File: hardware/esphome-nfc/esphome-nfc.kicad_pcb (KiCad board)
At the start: 4 copper layers, 68.2 x 41 mm, 20 parts, among them U1 ESP32-C3-WROOM-02, U2 PN7160A1HN/C100Y, U3 AMS1117-3.3, Y1 Crystal_GND24

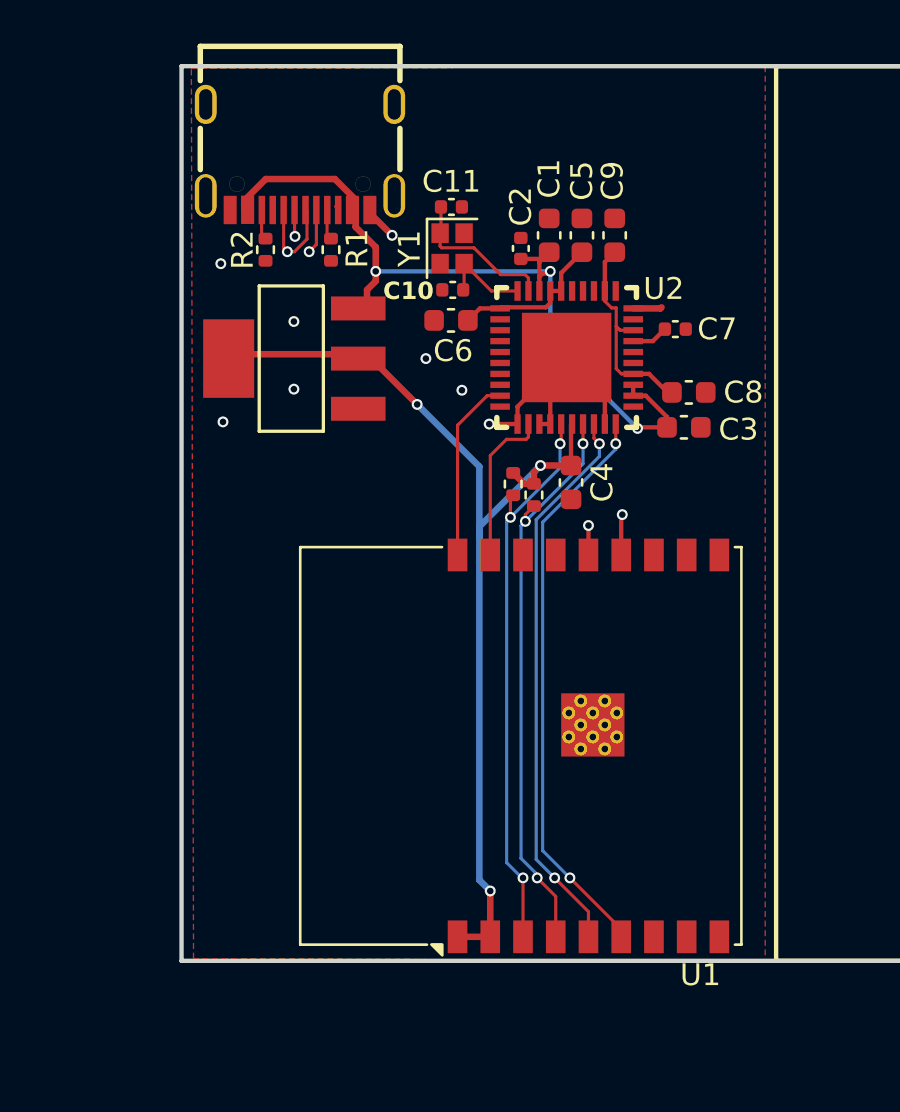
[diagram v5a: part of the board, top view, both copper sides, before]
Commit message: esphome-nfc: route & finalize everything except for NFC antenna and corresponding matching circuit
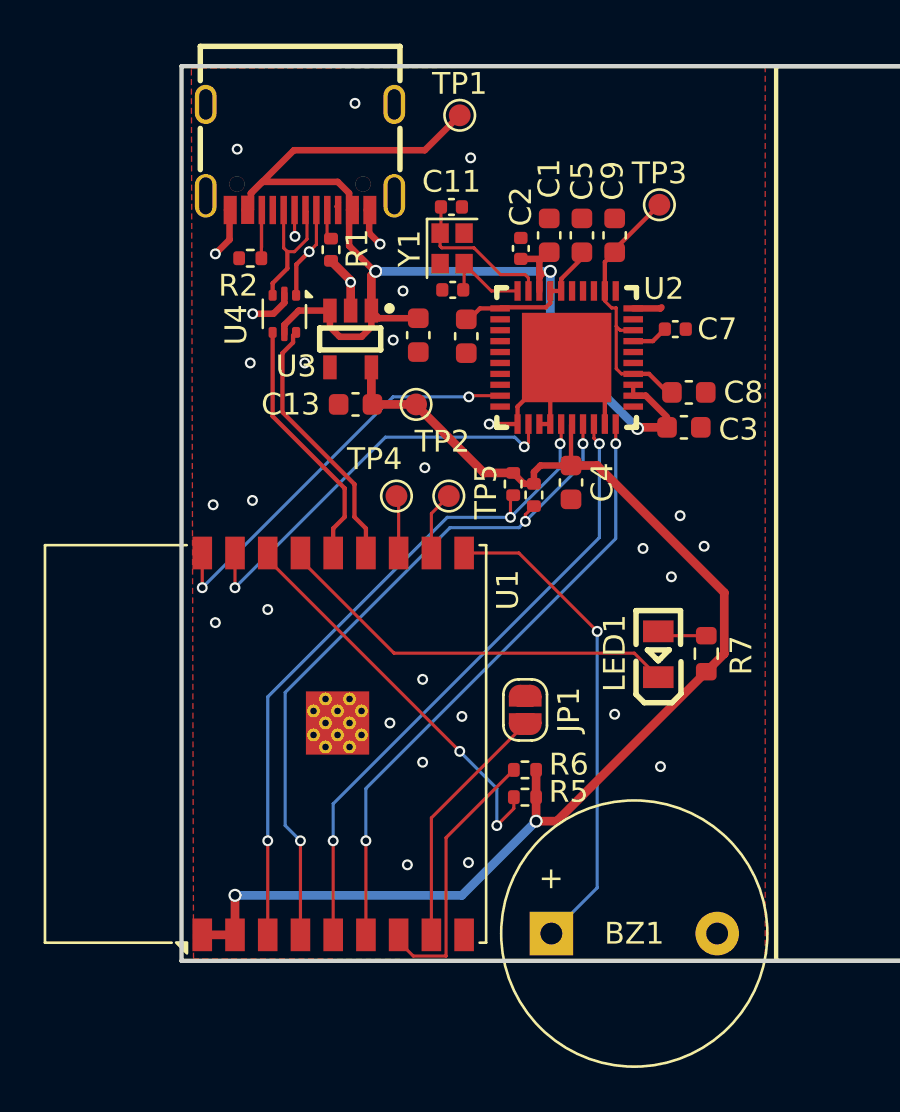
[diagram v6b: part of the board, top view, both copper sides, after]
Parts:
- added BZ1: Buzzer, Buzzer_Beeper:Buzzer_12x9.5RM7.6, F.Cu at (173.2, 113.8)
- added C12: 1.0 uF, Capacitor_SMD:C_0603_1608Metric, F.Cu at (167.1, 86.3)
- added C13: 1.0 uF, Capacitor_SMD:C_0603_1608Metric, F.Cu at (164.2, 89.5)
- added JP1: SolderJumper_2_Open, Jumper:SolderJumper-2_P1.3mm_Open_RoundedPad1.0x1.5mm, F.Cu at (172.0, 103.5)
- added LED1: 0805G (Green), easyeda2kicad:LED0805-R-RD, F.Cu at (178.1, 101.0)
- added R5: 10k, Resistor_SMD:R_0402_1005Metric, F.Cu at (172.0, 107.5)
- added R6: 10k, Resistor_SMD:R_0402_1005Metric, F.Cu at (172.0, 106.2)
- added R7: 100R, Resistor_SMD:R_0603_1608Metric, F.Cu at (180.3, 100.9)
- added TP1: ~, TestPoint:TestPoint_Pad_D1.0mm, F.Cu at (169.0, 76.2)
- added TP2: ~, TestPoint:TestPoint_Pad_D1.0mm, F.Cu at (167.0, 89.5)
- added TP3: ~, TestPoint:TestPoint_Pad_D1.0mm, F.Cu at (178.2, 80.3)
- added TP4: ~, TestPoint:TestPoint_Pad_D1.0mm, F.Cu at (166.1, 93.7)
- added TP5: ~, TestPoint:TestPoint_Pad_D1.0mm, F.Cu at (168.5, 93.7)
- added U4: USBLC6-2P6, Package_TO_SOT_SMD:SOT-666, F.Cu at (161.0, 85.3)
- U3: value AMS1117-3.3 -> AP2112K-3.3TRG1; footprint easyeda2kicad:SOT-223-3_L6.5-W3.4-P2.30-LS7.0-BR -> easyeda2kicad:SOT-25-5_L2.9-W1.6-P0.95-LS2.8-BL
- moved U1 11.7 mm to (163.2, 105.1)
- moved U3 2.77 mm to (164.0, 86.5), turned to 180 degrees
- moved C6 1.01 mm to (169.3, 86.4), turned to -90 degrees
- moved R2 0.80 mm to (159.4, 82.8), turned to 180 degrees
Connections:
- U1 pad 10: unconnected-(U1-IO10-Pad10) -> /BUZZER
- U1 pad 11: unconnected-(U1-IO20/RXD-Pad11) -> Net-(U1-IO20/RXD)
- U1 pad 12: unconnected-(U1-IO21/TXD-Pad12) -> Net-(U1-IO21/TXD)
- U1 pad 15: unconnected-(U1-IO3-Pad15) -> /LED
- U1 pad 16: unconnected-(U1-IO2-Pad16) -> Net-(U1-IO2)
- U1 pad 7: unconnected-(U1-IO8-Pad7) -> Net-(U1-IO8)
- U1 pad 8: unconnected-(U1-IO9-Pad8) -> Net-(JP1-A)
- U3 pad 1: GND -> +5V
- U3 pad 2: +3V3 -> GND
- U3 pad 4: +3V3 -> unconnected-(U3-NC-Pad4)
- USB2 pad 1: GND -> unconnected-(USB2-EP-Pad1)
- USB2 pad 2: GND -> unconnected-(USB2-EP-Pad2)
- USB2 pad 3: GND -> unconnected-(USB2-EP-Pad3)
- USB2 pad 4: GND -> unconnected-(USB2-EP-Pad4)
- USB2 pad A6: /D+ -> /DP
- USB2 pad A7: /D- -> /DN
- USB2 pad B6: /D+ -> /DP
- USB2 pad B7: /D- -> /DN
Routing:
- net /BUZZER: track 0.00 -> 22.3 mm, vias 0 -> 1
- net +5V: track 37.8 -> 57.5 mm
- net /LED: track 0.00 -> 18.9 mm
- net Net-(U1-IO2): track 0.00 -> 18.5 mm, vias 0 -> 2
- net /D+: track 26.1 -> 11.7 mm, vias 2 -> 0
- net /D-: track 25.9 -> 12.0 mm, vias 3 -> 0
- net +3V3: track 46.7 -> 59.8 mm, vias 3 -> 2
- net Net-(U1-IO8): track 0.00 -> 12.6 mm
- net /NFC_DWL: track 7.25 -> 19.0 mm, vias 0 -> 2
- net Net-(JP1-A): track 0.00 -> 11.4 mm
- net /NFC_WKUP: track 8.46 -> 18.9 mm, vias 0 -> 2
- net GND: track 16.1 -> 23.1 mm, vias 8 -> 29
- net /DP: track 0.00 -> 6.76 mm
- net /DN: track 0.00 -> 6.48 mm, vias 0 -> 2
- net /NFC_SCL: track 26.2 -> 32.1 mm
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
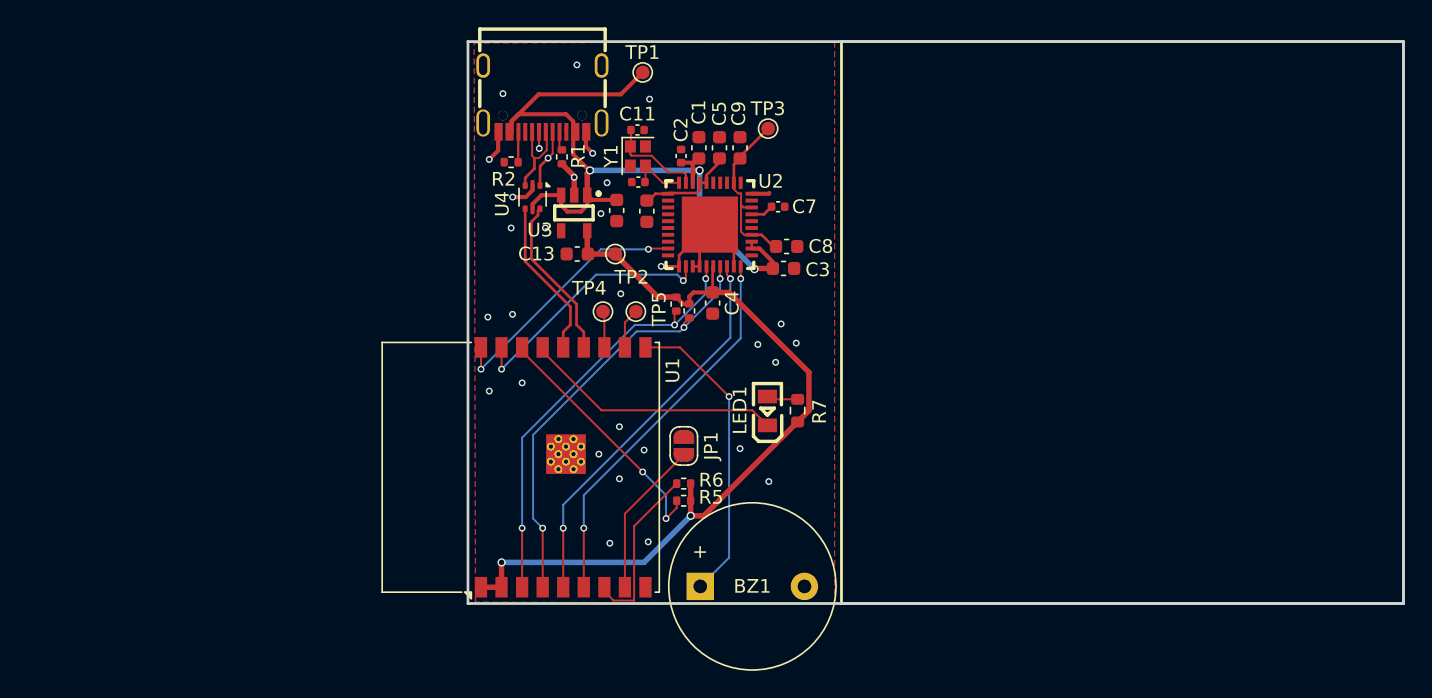
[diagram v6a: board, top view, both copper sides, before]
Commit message: esphome-nfc final touches
* Add an antenna and corresponding matching circuitry
* Add a button (you never know...)
* Mark components I plan to solder manually as "Do Not Place"
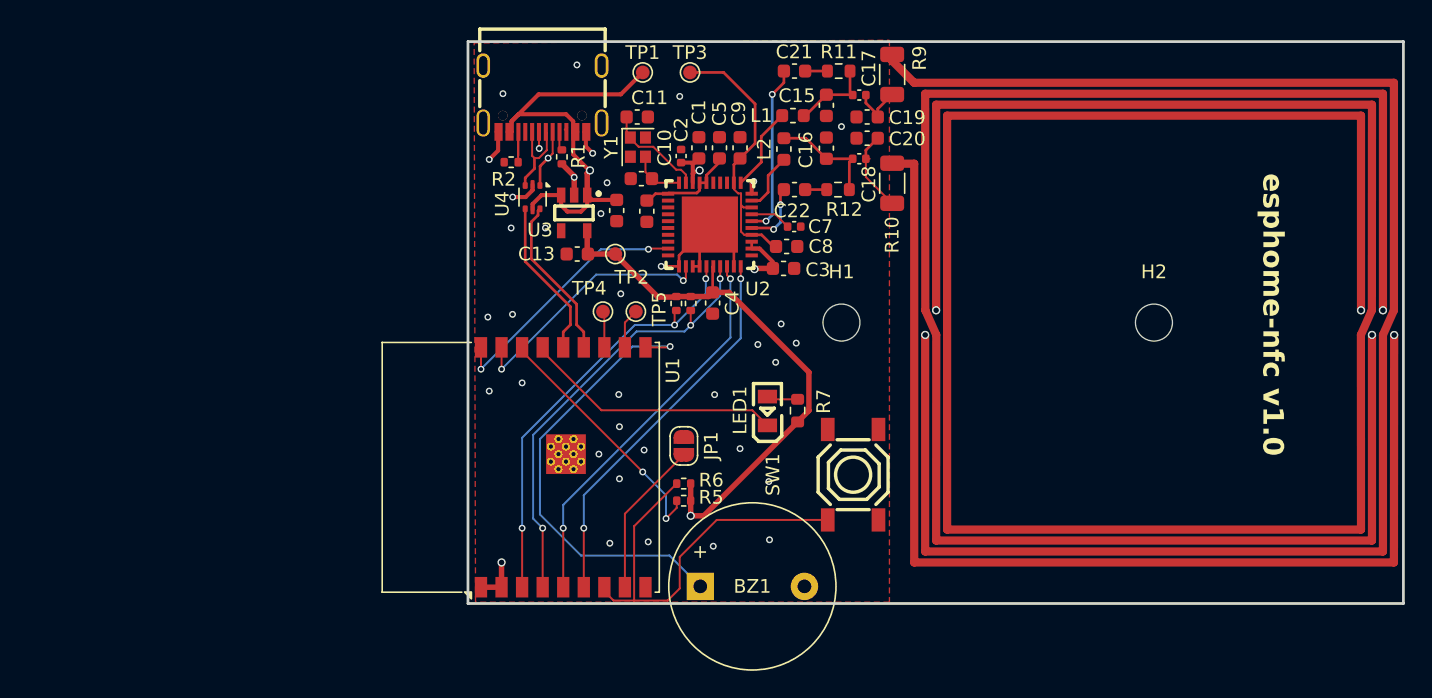
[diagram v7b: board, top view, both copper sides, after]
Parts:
- added C15: 330 pF, Capacitor_SMD:C_0603_1608Metric, F.Cu at (182.4, 78.7)
- added C16: 330 pF, Capacitor_SMD:C_0603_1608Metric, F.Cu at (182.4, 81.8)
- added C17: 75 pF, Capacitor_SMD:C_0402_1005Metric, F.Cu at (184.8, 77.9)
- added C18: 75 pF, Capacitor_SMD:C_0402_1005Metric, F.Cu at (184.8, 82.5)
- added C19: 150 pF, Capacitor_SMD:C_0603_1608Metric, F.Cu at (185.4, 79.5)
- added C20: 150 pF, Capacitor_SMD:C_0603_1608Metric, F.Cu at (185.4, 81.0)
- added C21: 1.0 uF, Capacitor_SMD:C_0603_1608Metric, F.Cu at (180.1, 76.2)
- added C22: 1.0 uF, Capacitor_SMD:C_0603_1608Metric, F.Cu at (180.1, 84.8)
- added H1: MountingHole, MountingHole:MountingHole_2.7mm_M2.5, F.Cu at (183.5, 94.5)
- added H2: MountingHole, MountingHole:MountingHole_2.7mm_M2.5, F.Cu at (206.3, 94.5)
- added L1: 160 nH, Inductor_SMD:L_0603_1608Metric, F.Cu at (180.0, 79.4)
- added L2: 160 nH, Inductor_SMD:L_0603_1608Metric, F.Cu at (179.3, 81.8)
- added R10: 2R0, Resistor_SMD:R_1206_3216Metric, F.Cu at (187.2, 84.3)
- added R11: 2.2K, Resistor_SMD:R_0603_1608Metric, F.Cu at (183.3, 76.2)
- added R12: 2.2K, Resistor_SMD:R_0603_1608Metric, F.Cu at (183.2, 84.8)
- added R9: 2R0, Resistor_SMD:R_1206_3216Metric, F.Cu at (187.2, 76.4)
- added SW1: TS-1187A-B-A-B, easyeda2kicad:SW-SMD_4P-L5.1-W5.1-P3.70-LS6.5-TL-2, F.Cu at (184.3, 105.6)
- C10, C11: footprint Capacitor_SMD:C_0402_1005Metric -> Capacitor_SMD:C_0603_1608Metric
- moved TP3 7.02 mm to (172.4, 76.2)
- moved C7 1.86 mm to (180.1, 87.5)
- moved C11 0.95 mm to (168.6, 79.5)
- moved Y1 0.65 mm to (168.7, 81.7)
- moved R4 0.55 mm to (172.5, 93.1)
- moved C10 0.33 mm to (168.9, 84.0)
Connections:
- net Net-(U1-IO8) renamed /BUTTON
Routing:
- net Net-(R9-Pad2): track 0.00 -> 521.0 mm, vias 0 -> 6
- net /BUTTON: track 12.6 -> 30.5 mm
- net /RXP: track 0.00 -> 12.5 mm, vias 0 -> 2
- net /BUZZER: track 22.3 -> 33.5 mm
- net Net-(C16-Pad2): track 0.00 -> 7.99 mm
- net /TVDD: track 12.5 -> 19.8 mm
- net Net-(C18-Pad2): track 0.00 -> 6.19 mm
- net /TX1: track 0.00 -> 6.15 mm
- net Net-(C15-Pad1): track 0.00 -> 6.04 mm
- net /RXN: track 0.00 -> 4.85 mm, vias 0 -> 2
- net /TX2: track 0.00 -> 4.30 mm
- net Net-(C17-Pad2): track 0.00 -> 3.88 mm
- net Net-(C21-Pad1): track 0.00 -> 1.62 mm
- net Net-(C22-Pad2): track 0.00 -> 1.58 mm
- net Net-(U2-VDD(VMID)): track 1.68 -> 2.99 mm
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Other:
- board text added: "esphome-nfc v1.0"
